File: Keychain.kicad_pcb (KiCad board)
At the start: 4 copper layers, 106.7 x 78.7 mm, 57 parts, among them J1 Micro_SD_Card, J2 Conn_01x04, U1 IMX6UL_BGA289, U2 DDR3_BGA96, U3 AZ1117C-3.3, U4 AZ1117C-1.5

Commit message: Finished first version of board
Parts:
- added J3: USB_A, Connector_USB:USB_A_Molex_67643_Horizontal, F.Cu at (137.0, 98.9)
- C1, C24, R4: moved to F.Cu
- moved C26 30.3 mm to (149.7, 86.1)
- moved C7 27.8 mm to (137.3, 86.5), turned to 90 degrees
- moved C22 26.8 mm to (138.3, 75.7), turned to 90 degrees
- moved J2 24.6 mm to (141.0, 66.9), turned to 270 degrees
- moved C6 23.9 mm to (130.7, 92.4)
- moved C1 21.5 mm to (137.3, 90.5), turned to 270 degrees
- moved U3 18.0 mm to (131.6, 87.7), turned to 0 degrees
- moved C20 16.5 mm to (129.1, 81.8)
- moved U4 12.2 mm to (131.7, 76.8), turned to 0 degrees
- moved C24 10.2 mm to (145.8, 76.7), turned to 180 degrees
- moved J1 4.68 mm to (157.4, 103.2)
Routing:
- net Debug_CTS: track 0.00 -> 27.8 mm
- net +5V: track 0.00 -> 26.0 mm
- net Debug_RTS: track 0.00 -> 24.9 mm
- net Debug_TX: track 0.00 -> 21.2 mm
- net Debug_RX: track 0.00 -> 20.5 mm
- net SD_D1: track 2.09 -> 15.4 mm, vias 0 -> 2
- net SD_D0: track 2.05 -> 15.3 mm, vias 0 -> 2
- net GND: track 111.4 -> 119.1 mm, vias 55 -> 64
- net SD_CMD: track 2.48 -> 10.2 mm, vias 0 -> 2
- net SD_D3: track 1.07 -> 8.07 mm, vias 0 -> 2
- net SD_CLK: track 3.26 -> 10.0 mm
- net SD_D2: track 2.40 -> 7.77 mm
- net +3V3: track 25.7 -> 29.6 mm, vias 9 -> 20
- net +1V5: track 34.9 -> 36.6 mm, vias 23 -> 33
- net /DDR/ZQPAD: vias 1 -> 2

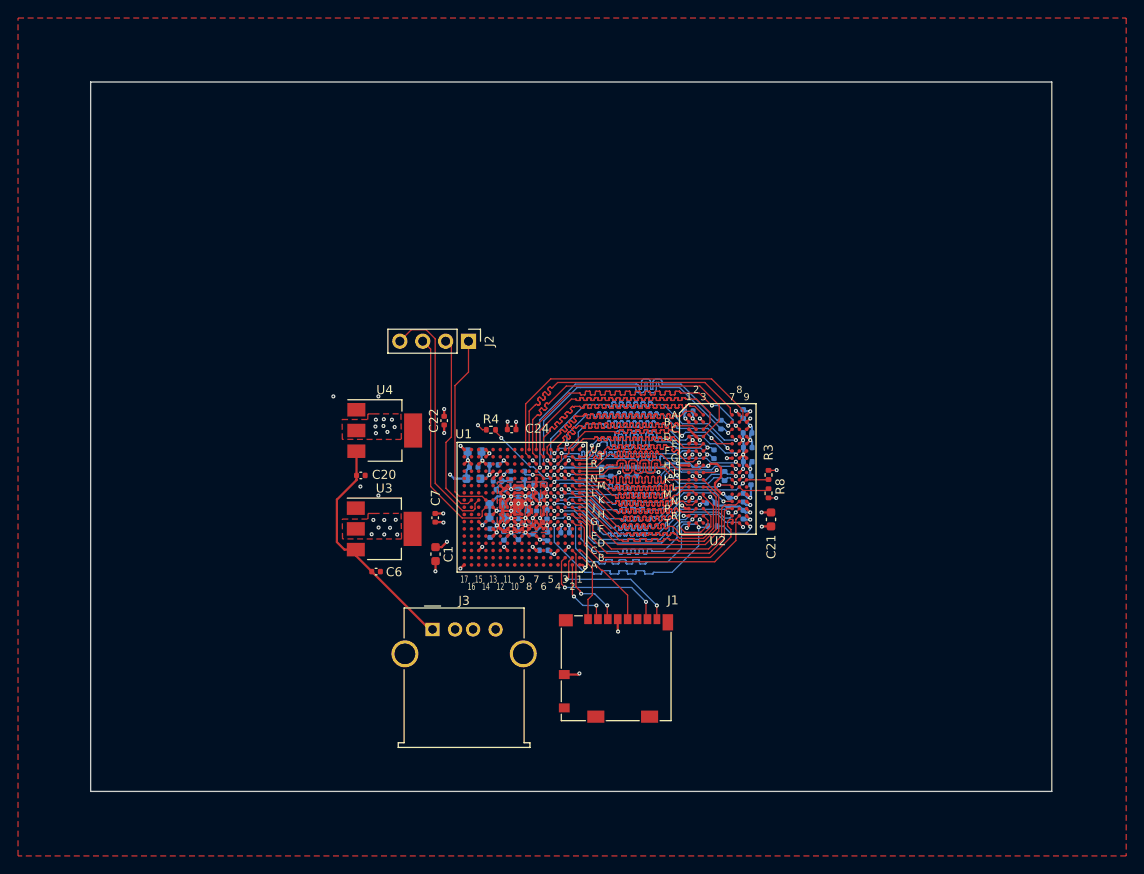
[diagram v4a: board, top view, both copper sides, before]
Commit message: Moved some parts to bottom for easier assembly
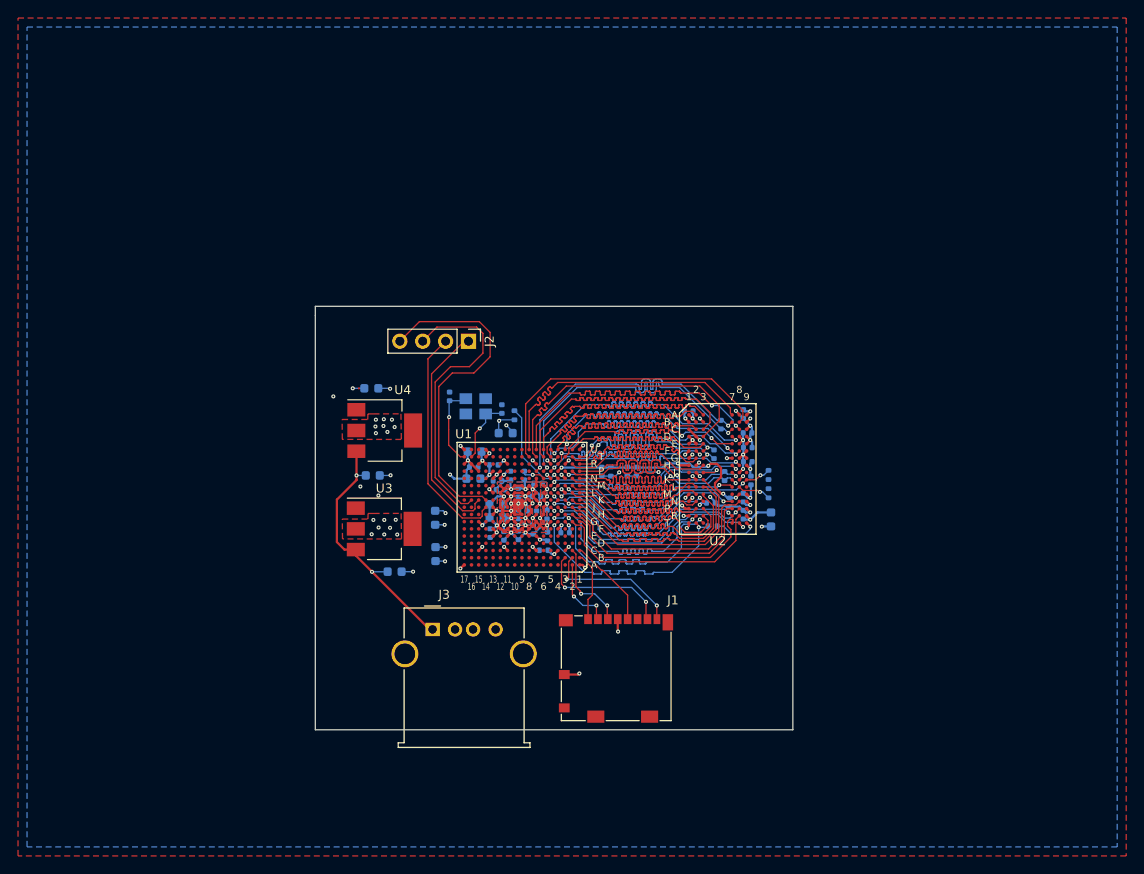
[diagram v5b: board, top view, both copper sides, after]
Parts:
- added C30: 18pF, Capacitor_SMD:C_0402_1005Metric, B.Cu at (138.9, 73.0)
- added C32: 18pF, Capacitor_SMD:C_0402_1005Metric, B.Cu at (144.7, 74.4)
- added Y1: Crystal_GND24, Crystal:Crystal_SMD_3225-4Pin_3.2x2.5mm, B.Cu at (141.8, 74.1)
- C1, C21, R3, R4, R8: moved to B.Cu
- C2, C4: value 4.7 -> 4.7uF
- C20, C22, C24, C6, C7: footprint Capacitor_SMD:C_0402_1005Metric -> Capacitor_SMD:C_0603_1608Metric; moved to B.Cu
- moved C22 8.85 mm to (130.2, 72.1), turned to 0 degrees
- moved R4 3.07 mm to (146.1, 75.1), turned to 90 degrees
- moved C6 2.06 mm to (132.8, 92.5)
- moved C20 1.32 mm to (130.4, 81.8)
- moved C24 0.78 mm to (145.1, 77.1)
- turned C1 to 90 degrees
- turned C21 to 270 degrees
- turned C7 to 270 degrees
- turned R3 to 270 degrees
- turned R8 to 270 degrees
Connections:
- J2 pad 1: Debug_TX -> Net-(J2-Pad1)
- J2 pad 2: Debug_RX -> Net-(J2-Pad2)
- J2 pad 3: Debug_RTS -> Net-(J2-Pad3)
- J2 pad 4: Debug_CTS -> Net-(J2-Pad4)
- U1 pad J14: Debug_RTS -> Net-(J2-Pad2)
- U1 pad K14: Debug_TX -> Net-(J2-Pad4)
- U1 pad K15: Debug_CTS -> Net-(J2-Pad1)
- U1 pad K16: Debug_RX -> Net-(J2-Pad3)
- U1 pad L13: Net-(U1-PadL13) -> +3V3
- U1 pad M13: Net-(U1-PadM13) -> +3V3
- U1 pad P15: Net-(U1-PadP15) -> GND
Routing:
- net Net-(J2-Pad4): track 0.00 -> 37.4 mm
- net Net-(J2-Pad3): track 0.00 -> 32.4 mm
- net Debug_CTS: track 27.8 -> 0.00 mm
- net Net-(J2-Pad2): track 0.00 -> 25.5 mm
- net Debug_RTS: track 24.9 -> 0.00 mm
- net Net-(J2-Pad1): track 0.00 -> 24.8 mm
- net Debug_TX: track 21.2 -> 0.00 mm
- net Debug_RX: track 20.5 -> 0.00 mm
- net Net-(C30-Pad1): track 0.00 -> 9.13 mm, vias 0 -> 1
- net Net-(C32-Pad1): track 0.00 -> 7.23 mm, vias 0 -> 1
- net GND: track 119.1 -> 122.7 mm, vias 64 -> 62
- net +5V: track 26.0 -> 28.8 mm, vias 0 -> 2
- net +1V5: track 36.6 -> 38.9 mm, vias 33 -> 32
- net /DDR/ZQPAD: track 9.67 -> 10.8 mm, vias 2 -> 1
- net +3V3: track 29.6 -> 30.6 mm, vias 20 -> 21
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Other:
- board size 106.7 x 78.7 mm -> 53 x 47 mm

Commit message: New layout!
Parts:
- removed C24: 10uF, Capacitor_SMD:C_0603_1608Metric
- removed C26, C28, C29, C31, C33, C35, C51, C52, C53, C54: 0.22uF, Capacitor_SMD:C_0402_1005Metric
- C1, C10, C11, C12, C13, C14, C15, C16, C17, C18, C19, C2, C20, C21, C22, C23, C25, C27, C3, C30, C32, C36, C37, C38, C39, C4, C44, C45, C46, C47, C5, C6, C7, C8, C9, R1, R3, R4, R5, R6, R7, R8, Y1: moved to F.Cu
- J2: footprint Connector_PinHeader_2.54mm:PinHeader_1x04_P2.54mm_Vertical -> Connector_PinHeader_2.54mm:PinHeader_1x05_P2.54mm_Vertical
- moved R1 23.5 mm to (145.1, 92.2), turned to 270 degrees
- moved J2 23.1 mm to (125.0, 83.5), turned to 0 degrees
- moved C8 16.7 mm to (133.9, 92.2), turned to 270 degrees
- moved C39 16.2 mm to (154.8, 79.2), turned to 90 degrees
- moved U3 15.8 mm to (124.2, 101.7), turned to 270 degrees
- moved C25 15.3 mm to (162.4, 71.9), turned to 0 degrees
- moved C7 15.1 mm to (125.9, 96.4), turned to 0 degrees
- moved C9 14.8 mm to (131.8, 89.5), turned to 180 degrees
- moved C12 14.6 mm to (132.9, 92.2), turned to 270 degrees
- moved C15 14.0 mm to (134.9, 92.2)
- moved C32 13.2 mm to (131.5, 74.7), turned to 0 degrees
- moved C13 13.2 mm to (131.8, 88.5), turned to 180 degrees
- moved C16 12.9 mm to (131.2, 87.2)
- moved C21 12.2 mm to (162.5, 88.5)
- moved C22 11.7 mm to (122.4, 80.8), turned to 180 degrees
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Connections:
- net /DDR/A0 renamed /A0
- net /DDR/A1 renamed /A1
- net /DDR/A10 renamed /A10
- net /DDR/A11 renamed /A11
- net /DDR/A12 renamed /A12
- net /DDR/A13 renamed /A13
- net /DDR/A14 renamed /A14
- net /DDR/A2 renamed /A2
- net /DDR/A3 renamed /A3
- net /DDR/A4 renamed /A4
- net /DDR/A5 renamed /A5
- net /DDR/A6 renamed /A6
- net /DDR/A7 renamed /A7
- net /DDR/A8 renamed /A8
- net /DDR/A9 renamed /A9
- net /DDR/BA0 renamed /BA0
- net /DDR/BA1 renamed /BA1
- net /DDR/BA2 renamed /BA2
- net /DDR/CAS# renamed /CAS#
- net /DDR/CK+ renamed /CK+
- net /DDR/CK- renamed /CK-
- net /DDR/CKE0 renamed /CKE0
- net /DDR/CS0# renamed /CS0#
- net /DDR/DML renamed /DML
- net /DDR/DMU renamed /DMU
- net /DDR/DQL0 renamed /DQL0
- net /DDR/DQL2 renamed /DQL2
- net /DDR/DQL3 renamed /DQL3
- net /DDR/DQL4 renamed /DQL4
- net /DDR/DQL5 renamed /DQL5
- net /DDR/DQSL+ renamed /DQSL+
- net /DDR/DQSL- renamed /DQSL-
- net /DDR/DQSU+ renamed /DQSU+
- net /DDR/DQSU- renamed /DQSU-
- net /DDR/DQU0 renamed /DQU0
- net /DDR/DQU2 renamed /DQU2
- net /DDR/DQU6 renamed /DQU6
- net /DDR/ODT0 renamed /ODT0
- net /DDR/RAS# renamed /RAS#
- net /DDR/RESET# renamed /RESET#
- net /DDR/WE# renamed /WE#
- net /DDR/ZQ renamed /ZQ
- net /DDR/ZQPAD renamed /ZQPAD
- net ARM_CAP renamed /ARM_CAP
- net HIGH_CAP renamed /HIGH_CAP
- net NVCC_PLL renamed /NVCC_PLL
- net Net-(C30-Pad1) renamed /XTALO
- net Net-(C32-Pad1) renamed /XTALI
- net SD_CLK renamed /SD_CLK
- net SD_CMD renamed /SD_CMD
- net SD_D0 renamed /SD_D0
- net SD_D1 renamed /SD_D1
- net SD_D2 renamed /SD_D2
- net SD_D3 renamed /SD_D3
- net SNVS_CAP renamed /SNVS_CAP
- net SOC_CAP renamed /SOC_CAP
- net VDD_HIGH_CAP renamed /VDD_HIGH_CAP
- C1 pad 1: +3V3 -> +1V5
- C2 pad 1: +3V3 -> +1V5
- C27 pad 1: +1V5 -> VREFDDR
- C3 pad 1: +3V3 -> +1V5
- C4 pad 1: +1V5 -> +3V3
- C5 pad 1: +3V3 -> +1V5
- J2 pad 1: Net-(J2-Pad1) -> /RX
- J2 pad 2: Net-(J2-Pad2) -> /CTS
- J2 pad 3: Net-(J2-Pad3) -> /TX
- J2 pad 4: Net-(J2-Pad4) -> /RTS
- U1 pad H10: +3V3 -> +1V5
- U1 pad H9: +3V3 -> +1V5
- U1 pad J10: +3V3 -> +1V5
- U1 pad J14: Net-(J2-Pad2) -> /RTS
- U1 pad J9: +3V3 -> +1V5
- U1 pad K10: +3V3 -> +1V5
- U1 pad K14: Net-(J2-Pad4) -> /TX
- U1 pad K15: Net-(J2-Pad1) -> /CTS
- U1 pad K16: Net-(J2-Pad3) -> /RX
- U1 pad K9: +3V3 -> +1V5
- U1 pad N13: +1V5 -> +3V3
- U1 pad P12: +1V5 -> +3V3
- U1 pad P3: /DDR/DQU5 -> /DQU5
- U1 pad P5: /DDR/DQU4 -> /DQU4
- U1 pad R1: /DDR/DQU7 -> /DQU7
- U1 pad R4: /DDR/DQU3 -> /DQU3
- U1 pad T5: /DDR/DQL6 -> /DQL6
- U1 pad U3: /DDR/DQU1 -> /DQU1
- U1 pad U4: /DDR/DQL7 -> /DQL7
- U1 pad U6: /DDR/DQL1 -> /DQL1
- U2 pad A2: /DDR/DQL6 -> /DQL7
- U2 pad A3: /DDR/DQL1 -> /DQL6
- U2 pad C2: /DDR/DQL7 -> /DQL1
- U2 pad F2: /DDR/DQU3 -> /DQU7
- U2 pad F7: /DDR/DQU1 -> /DQU3
- U2 pad G2: /DDR/DQU7 -> /DQU5
- U2 pad H7: /DDR/DQU5 -> /DQU4
- U2 pad H8: /DDR/DQU4 -> /DQU1
- U3 pad 1: GND -> Net-(U3-Pad1)
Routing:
- net GND: track 122.7 -> 84.0 mm, vias 62 -> 63
- net Net-(J2-Pad4): track 37.4 -> 0.00 mm
- net /DDR/DQL6: track 33.5 -> 0.00 mm
- net /DDR/DQL1: track 32.9 -> 0.00 mm
- net Net-(J2-Pad3): track 32.4 -> 0.00 mm
- net /DDR/DQU1: track 31.9 -> 0.00 mm, vias 2 -> 0
- net /DDR/DQL7: track 31.8 -> 0.00 mm
- net Net-(J2-Pad2): track 25.5 -> 0.00 mm
- net /DDR/DQU4: track 25.1 -> 0.00 mm, vias 2 -> 0
- net /DDR/DQU5: track 25.1 -> 0.00 mm, vias 2 -> 0
- net Net-(J2-Pad1): track 24.8 -> 0.00 mm
- net /DDR/DQU3: track 24.3 -> 0.00 mm, vias 2 -> 0
- net +5V: track 28.8 -> 52.7 mm, vias 2 -> 0
- net /DDR/DQU7: track 23.7 -> 0.00 mm
- net /DQU4: track 0.00 -> 22.5 mm, vias 0 -> 2
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- added copper zone on In2.Cu, net +1V5
- added copper zone on In2.Cu, net +3V3
- added copper zone on In1.Cu, net GND
- removed copper zone on PWR, net +1V5
- removed copper zone on B.Cu, net +3V3
- removed copper zone on F.Cu, net +3V3
- removed copper zone on PWR, net +3V3
- removed copper zone on B.Cu, net /ARM_CAP
- removed copper zone on B.Cu, net /SOC_CAP
- removed copper zone on GND, net GND
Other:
- board size 53 x 47 mm -> 48.5 x 40.1 mm
- net class DDR added: clearance 0.127, trace_width 0.145, via_dia 0.45, via_drill 0.2
- net class Default: trace_width 0.127 -> 0.1
- net class POWER added: clearance 0.127, trace_width 0.25, via_dia 0.45, via_drill 0.2
- rule pad_to_mask_clearance: 0 -> 0.05
- rule trace_min: 0.127 -> 0.1

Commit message: New layout
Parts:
- U3: value AZ1117C-3.3 -> AZ1117H-3.3
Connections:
- U3 pad 1: Net-(U3-Pad1) -> GND
- U3 pad 4: (no net) -> GND
- U4 pad 4: (no net) -> GND
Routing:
- net GND: track 84.0 -> 98.6 mm, vias 63 -> 86
- net (no net): vias 22 -> 0
- removed copper zone on B.Cu, net GND
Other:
- board size 48.5 x 40.1 mm -> 49.6 x 40.1 mm
- board text added: "CTS"
- board text added: "RTS"
- board text added: "RX"
- board text added: "TX"
